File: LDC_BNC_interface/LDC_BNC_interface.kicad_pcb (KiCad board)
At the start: 2 copper layers, 180 x 56 mm, 13 parts, among them J1 Conn_Coaxial, J2 Conn_Coaxial, J3 Conn_Coaxial, J4 DB25_Pins_MountingHoles, J5 Conn_Coaxial, J6 Conn_Coaxial, J7 Conn_Coaxial, J8 Conn_Coaxial, J9 Conn_Coaxial

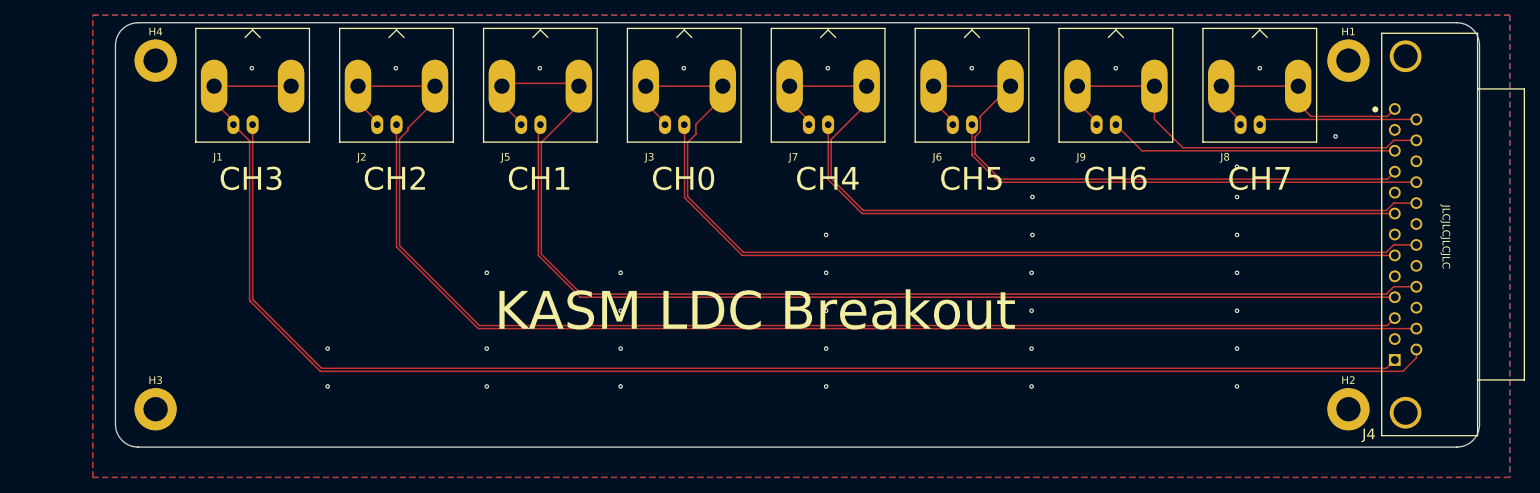
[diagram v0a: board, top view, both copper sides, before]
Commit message: Widened PCB
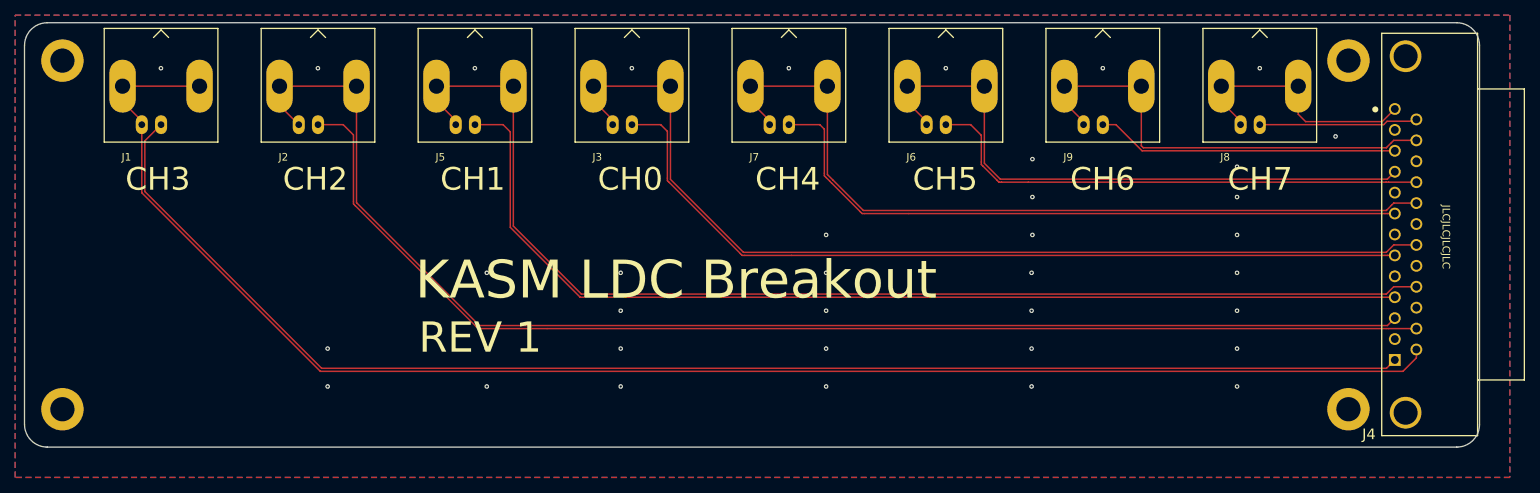
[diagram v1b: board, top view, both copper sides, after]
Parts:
- moved H3 12.3 mm to (53.0, 94.0)
- moved H4 12.3 mm to (53.0, 48.0)
- moved J1 12.1 mm to (66.0, 43.7)
- moved J2 10.4 mm to (86.7, 43.7)
- moved J5 8.63 mm to (107.4, 43.7)
- moved J3 6.91 mm to (128.1, 43.7)
- moved J7 5.18 mm to (148.8, 43.7)
- moved J6 3.45 mm to (169.6, 43.7)
- moved J9 1.73 mm to (190.3, 43.7)
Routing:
- net /IN3A: track 178.0 -> 184.8 mm
- net /IN2A: track 155.1 -> 161.4 mm
- net /IN1A: track 132.6 -> 138.2 mm
- net /IN0A: track 106.5 -> 111.6 mm
- net /IN3B: track 200.1 -> 205.1 mm
- net /IN4A: track 83.9 -> 88.4 mm
- net /IN6B: track 57.2 -> 61.0 mm
- net /IN5A: track 64.1 -> 67.5 mm
- net /IN5B: track 84.4 -> 81.9 mm
- net /IN4B: track 109.8 -> 108.0 mm
- net /IN6A: track 38.2 -> 40.0 mm
- net /IN7B: track 32.4 -> 33.8 mm
- net /IN1B: track 158.8 -> 158.0 mm
- net /IN2B: track 175.3 -> 175.8 mm
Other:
- board size 180 x 56 mm -> 192 x 56 mm
- board text added: "REV 1"
